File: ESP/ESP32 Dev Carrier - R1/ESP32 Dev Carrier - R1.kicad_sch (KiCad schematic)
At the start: 24 parts, among them J3 Conn_02x20_Top_Bottom, J4 Conn_01x05, J5 Conn_01x05, J6 Conn_01x05, SW1 SW_Push, U1 ESP32-WROVER-B_(16MB)

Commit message: Blurgh. Almost ready to order.
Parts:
- added D10, D11, D13, D14, D15, D5, D6, D9: BAT54S, Package_TO_SOT_SMD:SOT-23, symbol ESP32-Water-Meter-Monitor-rescue:D_Schottky_x2_Serial_AKC-Device
- added D16, D17: BAT54S, Package_TO_SOT_SMD:SOT-23, symbol Device:D_Schottky_x2_Serial_AKC
- added J10, J7, J8, J9: Conn_01x09, Connector_JST:JST_XH_B9B-XH-A_1x09_P2.50mm_Vertical, symbol Connector_Generic:Conn_01x09
- added J11, J12, J13, J14: Conn_01x04, Connector_JST:JST_XH_B4B-XH-A_1x04_P2.50mm_Vertical, symbol Connector_Generic:Conn_01x04
- added R18, R19, R20, R21, R22, R23: 4.7K, Resistor_SMD:R_0603_1608Metric, symbol Device:R_Small
- J4, J5, J6: footprint Connector_JST:JST_XH_B5B-XH-AM_1x05_P2.50mm_Vertical -> Connector_JST:JST_XH_B5B-XH-A_1x05_P2.50mm_Vertical
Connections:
- net +3V3: now also D10.2 (K), D11.2 (K), D13.2 (K), D14.2 (K), D15.2 (K), D16.2 (K), D17.2 (K), D5.2 (K), D6.2 (K), D9.2 (K), J10.2 (Pin_2), J11.2 (Pin_2), J12.2 (Pin_2), J13.2 (Pin_2), J14.2 (Pin_2), J7.2 (Pin_2), J8.2 (Pin_2), J9.2 (Pin_2), R18.2, R19.2, R20.2, R21.2, R22.2, R23.2
- net +5V: now also J10.1 (Pin_1), J11.1 (Pin_1), J12.1 (Pin_1), J13.1 (Pin_1), J14.1 (Pin_1), J7.1 (Pin_1), J8.1 (Pin_1), J9.1 (Pin_1)
- net GND: now also D10.1 (A), D11.1 (A), D13.1 (A), D14.1 (A), D15.1 (A), D16.1 (A), D17.1 (A), D5.1 (A), D6.1 (A), D9.1 (A), J10.9 (Pin_9), J11.4 (Pin_4), J12.4 (Pin_4), J13.4 (Pin_4), J14.4 (Pin_4), J7.9 (Pin_9), J8.9 (Pin_9), J9.9 (Pin_9)
- net IO2: now reaches J3.29 (Pin_29), R5.2, U1.24 (IO2/GPIO2/ADC2_CH2/TOUCH2/RTC_GPIO12/HSPIWP/HS2_DATA0/SD_DATA0)
- net at D2.1 (K), J3.20 (Pin_20), R14.1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: now also J4.3 (Pin_3), J5.3 (Pin_3), J6.3 (Pin_3); no longer J4.4 (Pin_4), J5.4 (Pin_4), J6.4 (Pin_4)
- net at D2.2 (K), J3.23 (Pin_23), R15.1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: now also J4.4 (Pin_4), J5.4 (Pin_4), J6.4 (Pin_4); no longer J4.3 (Pin_3), J5.3 (Pin_3), J6.3 (Pin_3)
- net at J3.11 (Pin_11), U1.8 (IO32/GPIO32/XTAL_32K_P/ADC1_CH4/TOUCH9/RTC_GPIO9): now also D10.3 (common), J10.5 (Pin_5), J7.5 (Pin_5), J8.5 (Pin_5), J9.5 (Pin_5); no longer R27.2
- net at J3.10 (Pin_10), U1.7 (IO35/GPIO35/ADC1_CH7/RTC_GPIO5): now also D14.3 (common), J7.4 (Pin_4), J8.4 (Pin_4), R20.1
- net at J3.12 (Pin_12), U1.9 (IO33/GPIO33/XTAL_32K_N/ADC1_CH5/TOUCH8/RTC_GPIO8): now also D9.3 (common), J10.6 (Pin_6), J7.6 (Pin_6), J8.6 (Pin_6), J9.6 (Pin_6)
- net at J3.13 (Pin_13), U1.10 (IO25/GPIO25/DAC_1/ADC2_CH8/RTC_GPIO6/EMAC_RXD0): now also D6.3 (common), J10.7 (Pin_7), J7.7 (Pin_7), J8.7 (Pin_7), J9.7 (Pin_7)
- net at J3.14 (Pin_14), U1.11 (IO26/DAC_2/ADC2_CH9/RTC_GPIO7/EMAC_RXD1): now also D5.3 (common), J10.8 (Pin_8), J7.8 (Pin_8), J8.8 (Pin_8), J9.8 (Pin_8)
- net at J3.15 (Pin_15), U1.12 (IO27/GPIO27/ADC2_CH7/TOUCH7/RTC_GPIO17/EMAC_RX_DV): now also R27.2
- net at J3.24 (Pin_24), U1.31 (IO19/GPIO19/VSPIQ/U0CTS/EMAC_TXD0): now also D16.3 (common), J11.3 (Pin_3), J12.3 (Pin_3), R22.1
- net at J3.25 (Pin_25), U1.30 (IO18/GPIO18/VSPICLK/HS1_DATA7): now also D17.3 (common), J13.3 (Pin_3), J14.3 (Pin_3), R23.1
- net at J3.26 (Pin_26), U1.29 (IO5/GPIO5/VSPICS0/HS1_DATA6/EMAC_RX_CLK): now also D11.3 (common), J10.3 (Pin_3), J9.3 (Pin_3), R18.1
- net IO4: now reaches J3.27 (Pin_27), U1.26 (IO4/GPIO4/ADC2_CH0/TOUCH0/RTC_GPIO10/HSPIHD/HS2_DATA1/SD_DATA1/EMAC_TX_ER)
- net at J3.30 (Pin_30), U1.23 (IO15/GPIO15/ADC2_CH3/TOUCH3/MTDO/HSPICS0/RTC_GPIO13/HS2_CMD/SD_CMD/EMAC_RXD3): now also D13.3 (common), J10.4 (Pin_4), J9.4 (Pin_4), R19.1
- net at J3.9 (Pin_9), U1.6 (IO34/GPIO34/ADC1_CH6/RTC_GPIO4): now also D15.3 (common), J7.3 (Pin_3), J8.3 (Pin_3), R21.1
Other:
- moved on the sheet: D12, D2, J4, J5, J6, R10, R14, R15

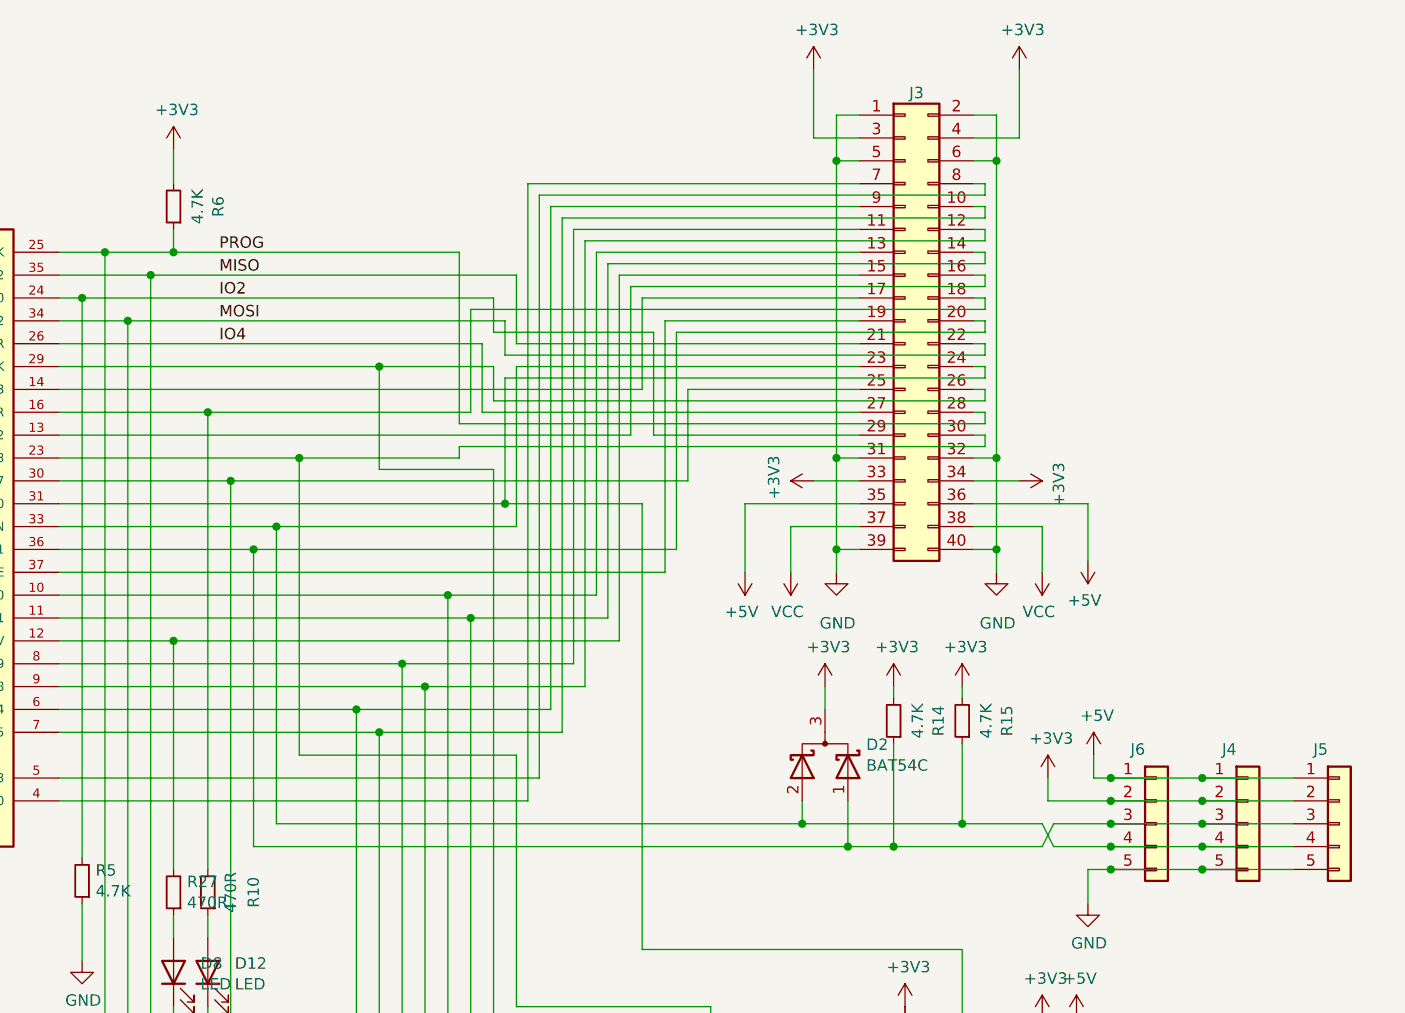
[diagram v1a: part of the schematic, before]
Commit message: Reworking things to use the new controller PCB.
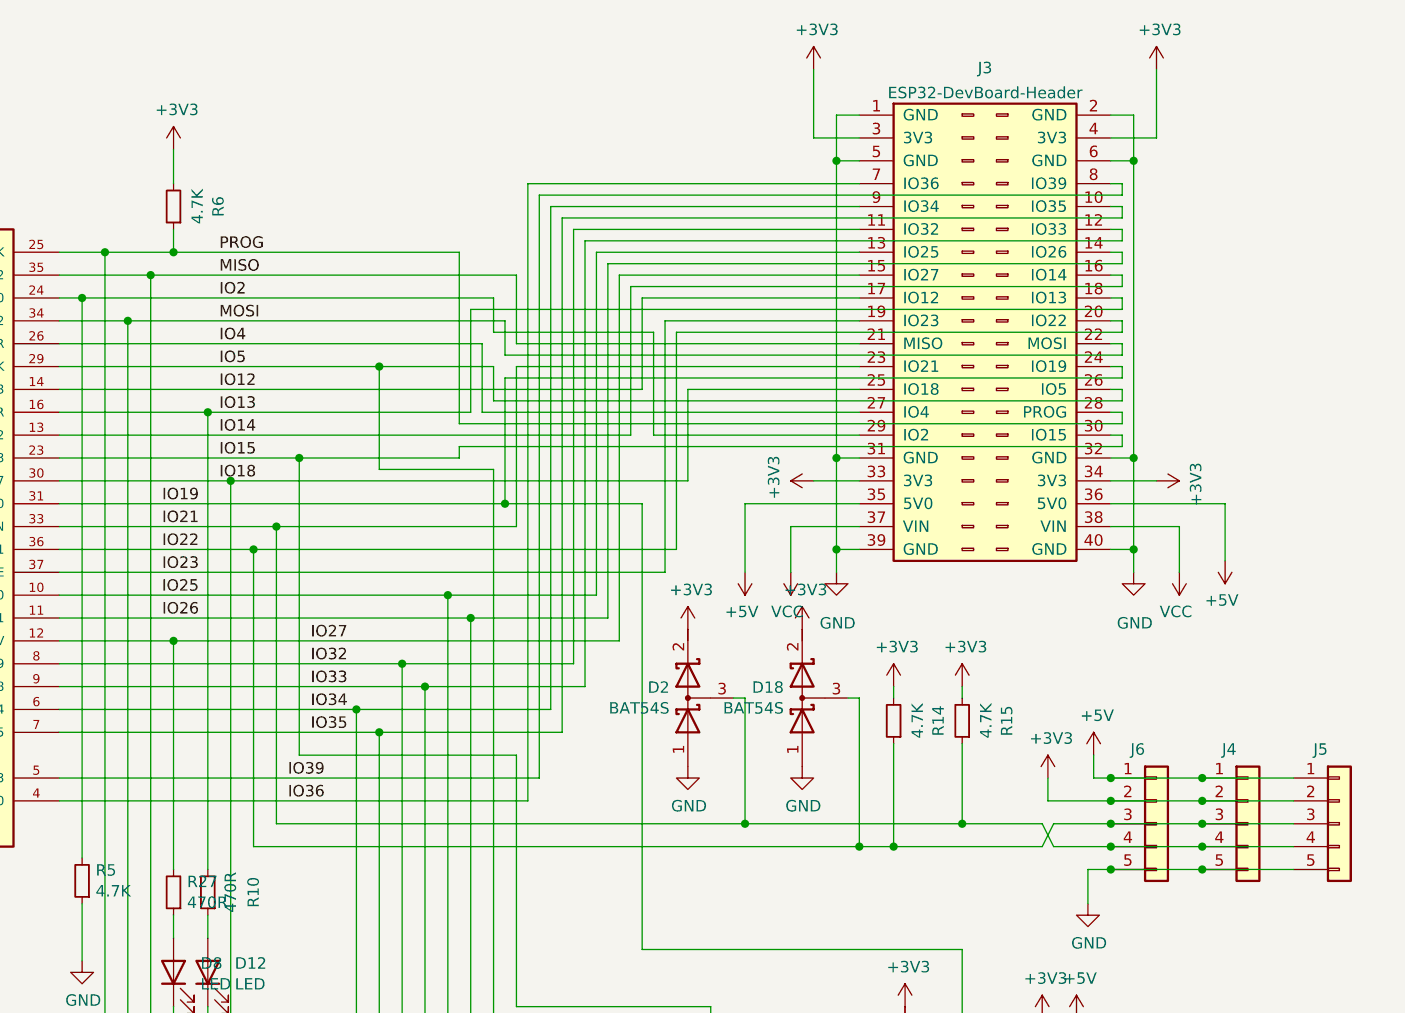
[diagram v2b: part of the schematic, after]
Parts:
- removed D2: BAT54C, Package_TO_SOT_SMD:SOT-23, symbol Device:D_Schottky_x2_KCom_AAK_Parallel
- removed J3: Conn_02x20_Top_Bottom, Connector_PinHeader_2.54mm:PinHeader_2x20_P2.54mm_Vertical, symbol Connector_Generic:Conn_02x20_Odd_Even
- added D18, D2: BAT54S, Package_TO_SOT_SMD:SOT-23, symbol Device:D_Schottky_x2_Serial_AKC
- added J3: ESP32-DevBoard-Header, Connector_PinHeader_2.54mm:PinHeader_2x20_P2.54mm_Vertical, symbol connectors:ESP32-DevBoard-Header
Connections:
- net +3V3: now also D18.2 (K), D2.2 (K), J3.3 (3V3), J3.33 (3V3), J3.34 (3V3), J3.4 (3V3)
- net +5V: now also J3.35 (5V0), J3.36 (5V0)
- net GND: now also D18.1 (A), D2.1 (A), J3.1 (GND), J3.2 (GND), J3.31 (GND), J3.32 (GND), J3.39 (GND), J3.40 (GND), J3.5 (GND), J3.6 (GND)
- net IO2: now also J3.29 (IO2)
- net IO4: now also J3.27 (IO4)
- net MISO: now also J3.21 (MISO)
- net MOSI: now also J3.22 (MOSI)
- net PROG: now also J3.28 (PROG)
- net VCC: now also J3.37 (VIN), J3.38 (VIN)
- net IO22: now reaches J4.3 (Pin_3), J5.3 (Pin_3), J6.3 (Pin_3), R14.1, U1.36 (IO22/GPIO22/VSPIWP/U0RTS/EMAC_TXD1)
- net IO22: now also D18.3 (common), J3.20 (IO22)
- net IO21: now reaches J4.4 (Pin_4), J5.4 (Pin_4), J6.4 (Pin_4), R15.1, U1.33 (IO21/GPIO21/VSPIHD/EMAC_TX_EN)
- net IO21: now also D2.3 (common), J3.23 (IO21)
- net IO13: now reaches R10.2, U1.16 (IO13/GPIO13/ADC2_CH4/TOUCH4/RTC_GPIO14/MTCK/HSPID/HS2_DATA3/SD_DATA3/EMAC_RX_ER)
- net IO13: now also J3.18 (IO13)
- net IO27: now reaches R27.2, U1.12 (IO27/GPIO27/ADC2_CH7/TOUCH7/RTC_GPIO17/EMAC_RX_DV)
- net IO27: now also J3.15 (IO27)
- net IO35: now reaches D14.3 (common), J7.4 (Pin_4), J8.4 (Pin_4), R20.1, U1.7 (IO35/GPIO35/ADC1_CH7/RTC_GPIO5)
- net IO35: now also J3.10 (IO35)
- net IO18: now reaches D17.3 (common), J13.3 (Pin_3), J14.3 (Pin_3), R23.1, U1.30 (IO18/GPIO18/VSPICLK/HS1_DATA7)
- net IO18: now also J3.25 (IO18)
- net IO34: now reaches D15.3 (common), J7.3 (Pin_3), J8.3 (Pin_3), R21.1, U1.6 (IO34/GPIO34/ADC1_CH6/RTC_GPIO4)
- net IO34: now also J3.9 (IO34)
- net IO32: now reaches D10.3 (common), J10.5 (Pin_5), J7.5 (Pin_5), J8.5 (Pin_5), J9.5 (Pin_5), U1.8 (IO32/GPIO32/XTAL_32K_P/ADC1_CH4/TOUCH9/RTC_GPIO9)
- net IO32: now also J3.11 (IO32)
- net IO33: now reaches D9.3 (common), J10.6 (Pin_6), J7.6 (Pin_6), J8.6 (Pin_6), J9.6 (Pin_6), U1.9 (IO33/GPIO33/XTAL_32K_N/ADC1_CH5/TOUCH8/RTC_GPIO8)
- net IO33: now also J3.12 (IO33)
- net IO25: now reaches D6.3 (common), J10.7 (Pin_7), J7.7 (Pin_7), J8.7 (Pin_7), J9.7 (Pin_7), U1.10 (IO25/GPIO25/DAC_1/ADC2_CH8/RTC_GPIO6/EMAC_RXD0)
- net IO25: now also J3.13 (IO25)
- net IO26: now reaches D5.3 (common), J10.8 (Pin_8), J7.8 (Pin_8), J8.8 (Pin_8), J9.8 (Pin_8), U1.11 (IO26/DAC_2/ADC2_CH9/RTC_GPIO7/EMAC_RXD1)
- net IO26: now also J3.14 (IO26)
- net IO19: now reaches D16.3 (common), J11.3 (Pin_3), J12.3 (Pin_3), R22.1, U1.31 (IO19/GPIO19/VSPIQ/U0CTS/EMAC_TXD0)
- net IO19: now also J3.24 (IO19)
- net IO5: now reaches D11.3 (common), J10.3 (Pin_3), J9.3 (Pin_3), R18.1, U1.29 (IO5/GPIO5/VSPICS0/HS1_DATA6/EMAC_RX_CLK)
- net IO5: now also J3.26 (IO5)
- net IO15: now reaches D13.3 (common), J10.4 (Pin_4), J9.4 (Pin_4), R19.1, U1.23 (IO15/GPIO15/ADC2_CH3/TOUCH3/MTDO/HSPICS0/RTC_GPIO13/HS2_CMD/SD_CMD/EMAC_RXD3)
- net IO15: now also J3.30 (IO15)
- net IO14: now reaches U1.13 (IO14/GPIO14/ADC2_CH6/TOUCH6/RTC_GPIO16/MTMS/HSPICLK/HS2_CLK/SD_CLK/EMAC_TXD2)
- net IO14: now also J3.16 (IO14)
- net IO12: now reaches U1.14 (IO12/GPIO12/ADC2_CH5/TOUCH5/RTC_GPIO15/HSPIQ/HS2_DATA2/SD_DATA2/EMAC_TXD3)
- net IO12: now also J3.17 (IO12)
- net IO23: now reaches U1.37 (IO23/GPIO23/VSPID/HS1_STROBE)
- net IO23: now also J3.19 (IO23)
- net IO36: now reaches U1.4 (SENSOR_VP/GPIO36/ADC1_CH0/RTC_GPIO0)
- net IO36: now also J3.7 (IO36)
- net IO39: now reaches U1.5 (SENSOR_VN/GPIO39/ADC1_CH3/RTC_GPIO3)
- net IO39: now also J3.8 (IO39)
